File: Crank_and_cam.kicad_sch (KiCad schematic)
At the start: 17 parts, among them IC1 Trig Cond Socket, IC2 Trig Cond Socket

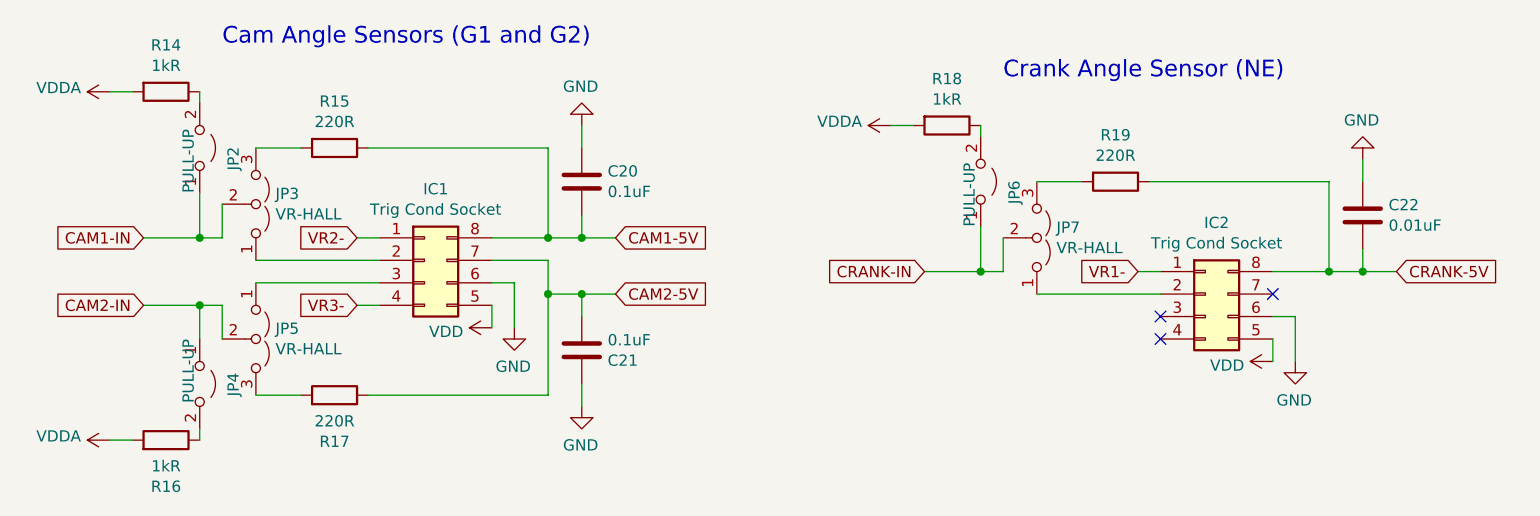
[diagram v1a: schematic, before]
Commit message: Swapped which angle sensors are connected to VR conditioners
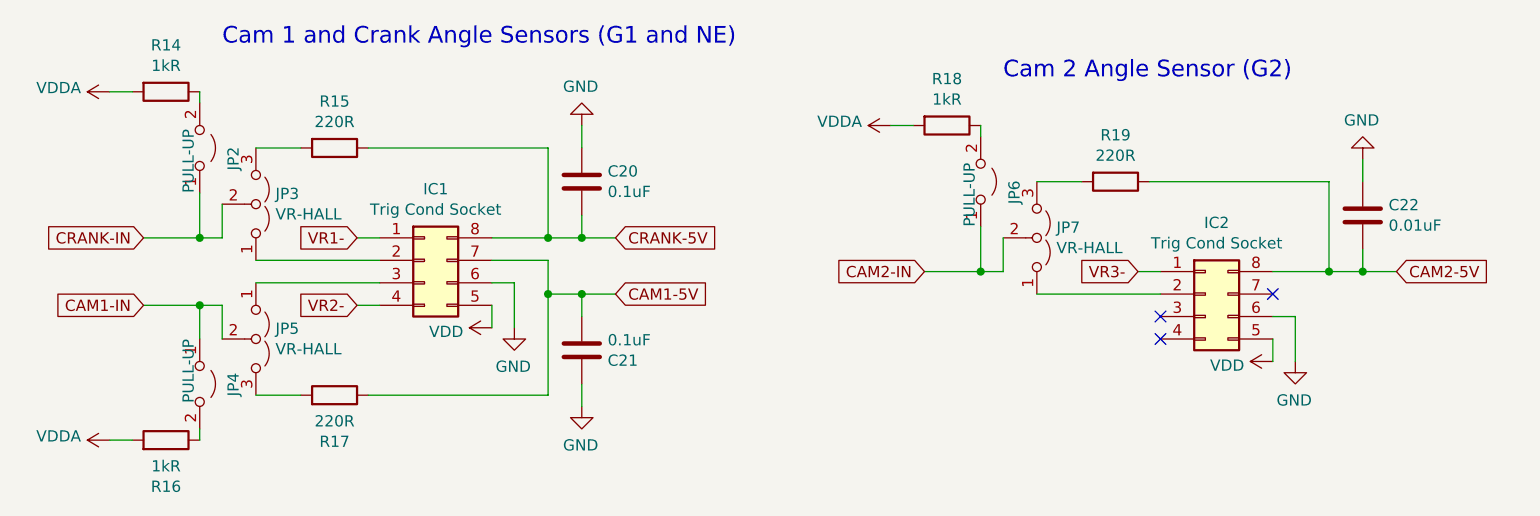
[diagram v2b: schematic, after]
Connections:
- net CAM1-5V: now also C21.2, IC1.7 (Pin_7), R17.1; no longer C20.2, IC1.8 (Pin_8), R15.1
- net CAM1-IN: now also JP4.1 (A), JP5.2 (C); no longer JP2.1 (A), JP3.2 (C)
- net CAM2-5V: now also C22.2, IC2.8 (Pin_8), R19.1; no longer C21.2, IC1.7 (Pin_7), R17.1
- net CAM2-IN: now also JP6.1 (A), JP7.2 (C); no longer JP4.1 (A), JP5.2 (C)
- net CRANK-5V: now also C20.2, IC1.8 (Pin_8), R15.1; no longer C22.2, IC2.8 (Pin_8), R19.1
- net CRANK-IN: now also JP2.1 (A), JP3.2 (C); no longer JP6.1 (A), JP7.2 (C)
- net VR1-: now also IC1.1 (Pin_1); no longer IC2.1 (Pin_1)
- net VR2-: now also IC1.4 (Pin_4); no longer IC1.1 (Pin_1)
- net VR3-: now also IC2.1 (Pin_1); no longer IC1.4 (Pin_4)
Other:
- note added: "Cam 1 and Crank Angle Sensors (G1 and NE)"
- note added: "Cam 2 Angle Sensor (G2)"
- note removed: "Cam Angle Sensors (G1 and G2)"
- note removed: "Crank Angle Sensor (NE)"
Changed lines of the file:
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@@
     (stroke (width 0) (type default) (color 0 0 0 0))
   )
-  (text "Cam Angle Sensors (G1 and G2)" (at 45.085 21.59 0)
+  (text "Cam 1 and Crank Angle Sensors (G1 and NE)" (at 45.085 21.59 0)
     (effects (font (size 1.8796 1.8796)) (justify left bottom))
   )
-  (text "Crank Angle Sensor (NE)" (at 133.35 25.4 0)
+  (text "Cam 2 Angle Sensor (G2)" (at 133.35 25.4 0)
     (effects (font (size 1.8796 1.8796)) (justify left bottom))
   )
-  (global_label "VR2-" (shape input) (at 60.325 43.18 180) (fields_autoplaced)
+  (global_label "VR1-" (shape input) (at 60.325 43.18 180) (fields_autoplaced)
     (effects (font (size 1.27 1.27)) (justify right))
     (property "Intersheet References" "${INTERSHEET_REFS}" (id 0) (at 52.7714 43.1006 0)
@@
     )
   )
-  (global_label "CAM1-5V" (shape input) (at 89.535 43.18 0) (fields_autoplaced)
+  (global_label "CRANK-5V" (shape input) (at 89.535 43.18 0) (fields_autoplaced)
     (effects (font (size 1.27 1.27)) (justify left))
-    (property "Intersheet References" "${INTERSHEET_REFS}" (id 0) (at 100.8381 43.1006 0)
+    (property "Intersheet References" "${INTERSHEET_REFS}" (id 0) (at 102.0476 43.1006 0)
       (effects (font (size 1.27 1.27)) (justify left) hide)
     )
   )
-  (global_label "CAM1-IN" (shape input) (at 36.195 43.18 180) (fields_autoplaced)
+  (global_label "CRANK-IN" (shape input) (at 36.195 43.18 180) (fields_autoplaced)
     (effects (font (size 1.27 1.27)) (justify right))
-    (property "Intersheet References" "${INTERSHEET_REFS}" (id 0) (at 0 0 0)
-      (effects (font (size 1.27 1.27)) hide)
+    (property "Intersheet References" "${INTERSHEET_REFS}" (id 0) (at 24.0452 43.1006 0)
+      (effects (font (size 1.27 1.27)) (justify right) hide)
     )
   )
-  (global_label "CRANK-IN" (shape input) (at 124.46 46.99 180) (fields_autoplaced)
+  (global_label "CAM2-IN" (shape input) (at 124.46 46.99 180) (fields_autoplaced)
     (effects (font (size 1.27 1.27)) (justify right))
-    (property "Intersheet References" "${INTERSHEET_REFS}" (id 0) (at 0.635 0 0)
-      (effects (font (size 1.27 1.27)) hide)
+    (property "Intersheet References" "${INTERSHEET_REFS}" (id 0) (at 113.5198 46.9106 0)
+      (effects (font (size 1.27 1.27)) (justify right) hide)
     )
   )
-  (global_label "VR3-" (shape input) (at 60.325 50.8 180) (fields_autoplaced)
+  (global_label "VR2-" (shape input) (at 60.325 50.8 180) (fields_autoplaced)
     (effects (font (size 1.27 1.27)) (justify right))
     (property "Intersheet References" "${INTERSHEET_REFS}" (id 0) (at 52.7714 50.7206 0)
@@
     )
   )
-  (global_label "CRANK-5V" (shape input) (at 177.8 46.99 0) (fields_autoplaced)
+  (global_label "CAM2-5V" (shape input) (at 177.8 46.99 0) (fields_autoplaced)
     (effects (font (size 1.27 1.27)) (justify left))
-    (property "Intersheet References" "${INTERSHEET_REFS}" (id 0) (at 190.3126 46.9106 0)
+    (property "Intersheet References" "${INTERSHEET_REFS}" (id 0) (at 189.1031 46.9106 0)
       (effects (font (size 1.27 1.27)) (justify left) hide)
     )
   )
-  (global_label "CAM2-5V" (shape input) (at 89.535 49.53 0) (fields_autoplaced)
+  (global_label "CAM1-5V" (shape input) (at 89.535 49.53 0) (fields_autoplaced)
     (effects (font (size 1.27 1.27)) (justify left))
     (property "Intersheet References" "${INTERSHEET_REFS}" (id 0) (at 100.8381 49.4506 0)
@@
     )
   )
-  (global_label "VR1-" (shape input) (at 148.59 46.99 180) (fields_autoplaced)
+  (global_label "VR3-" (shape input) (at 148.59 46.99 180) (fields_autoplaced)
     (effects (font (size 1.27 1.27)) (justify right))
     (property "Intersheet References" "${INTERSHEET_REFS}" (id 0) (at 141.0364 46.9106 0)
@@
     )
   )
-  (global_label "CAM2-IN" (shape input) (at 36.195 50.8 180) (fields_autoplaced)
+  (global_label "CAM1-IN" (shape input) (at 36.195 50.8 180) (fields_autoplaced)
     (effects (font (size 1.27 1.27)) (justify right))
-    (property "Intersheet References" "${INTERSHEET_REFS}" (id 0) (at 0 0 0)
-      (effects (font (size 1.27 1.27)) hide)
+    (property "Intersheet References" "${INTERSHEET_REFS}" (id 0) (at 25.2548 50.7206 0)
+      (effects (font (size 1.27 1.27)) (justify right) hide)
     )
   )
